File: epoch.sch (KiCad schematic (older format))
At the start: 30 parts, among them J1 USB_OTG, J2 CONN_01X05, P3 CONN_01X10, SW1 SW_Reset, SW2 SW_Up, SW3 SW_Middle, SW4 SW_Down, U1 MIC5219-3.3BM5, U2 ATSAMD21Ennc-AU, U3 DS3231MZ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

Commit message: Wire up
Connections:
- net INTC: now also U2.14 (PA11); no longer U2.25 (PA27)
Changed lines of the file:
@@
 Wire Wire Line
 	5550 2400 5550 2600
-Text GLabel 3750 5600 2    60   Input ~ 0
+Text GLabel 3750 4500 2    60   Input ~ 0
 INTC
 $EndSCHEMATC

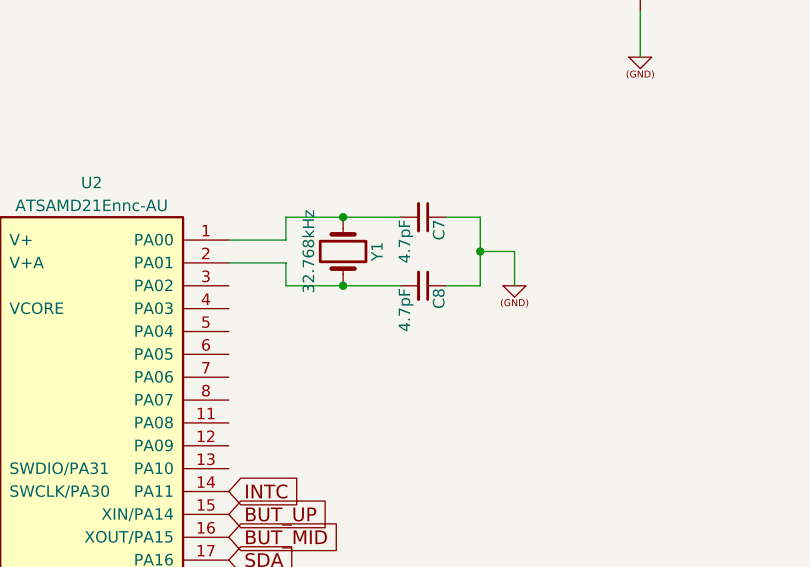
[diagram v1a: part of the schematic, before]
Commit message: Update resonator crystal to 18pF and create BOM csv
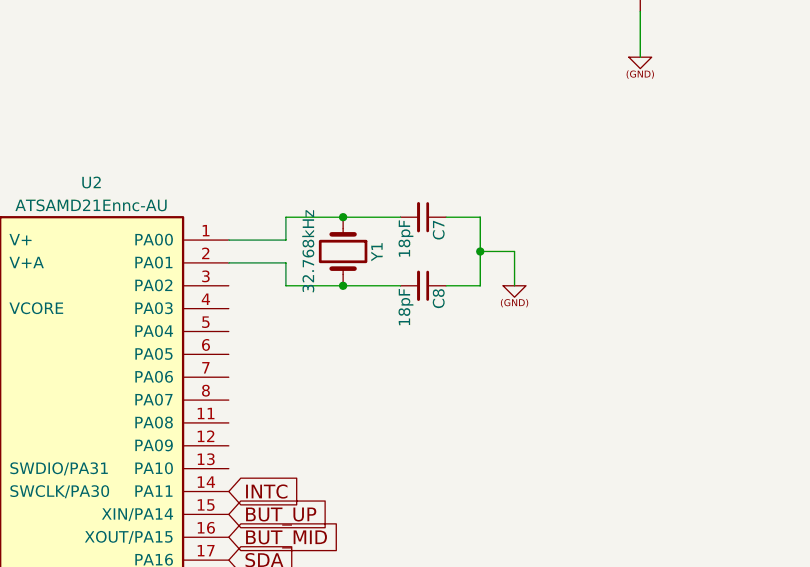
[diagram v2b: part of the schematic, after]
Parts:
- C7, C8: value 4.7pF -> 18pF
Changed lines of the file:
@@
 P 4600 3300
 F 0 "C7" H 4610 3370 50  0000 L CNN
-F 1 "4.7pF" H 4610 3220 50  0000 L CNN
+F 1 "18pF" H 4610 3220 50  0000 L CNN
 F 2 "Capacitors_SMD:C_0805_HandSoldering" H 4600 3300 50  0001 C CNN
 F 3 "" H 4600 3300 50  0000 C CNN
@@
 P 4600 3600
 F 0 "C8" H 4610 3670 50  0000 L CNN
-F 1 "4.7pF" H 4610 3520 50  0000 L CNN
+F 1 "18pF" H 4610 3520 50  0000 L CNN
 F 2 "Capacitors_SMD:C_0805_HandSoldering" H 4600 3600 50  0001 C CNN
 F 3 "" H 4600 3600 50  0000 C CNN

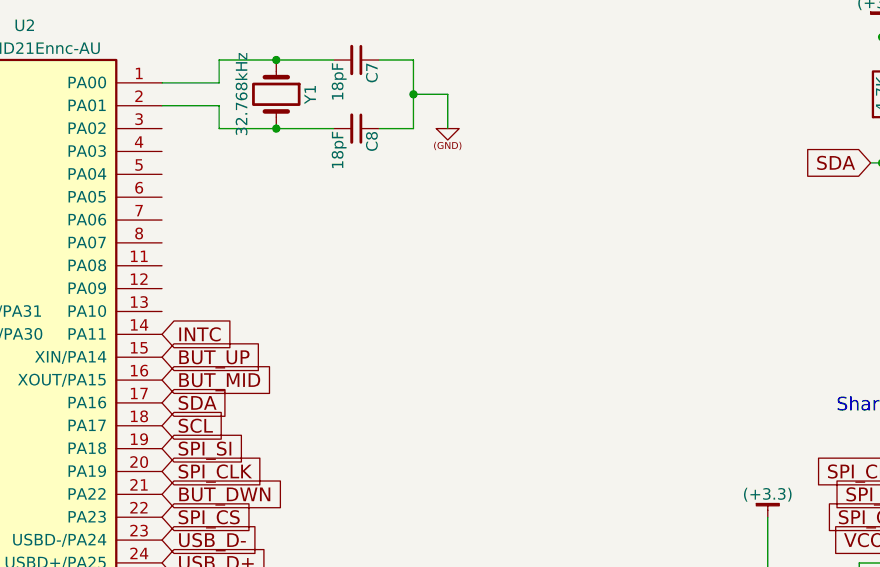
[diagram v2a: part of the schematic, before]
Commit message: Round corners and add LED
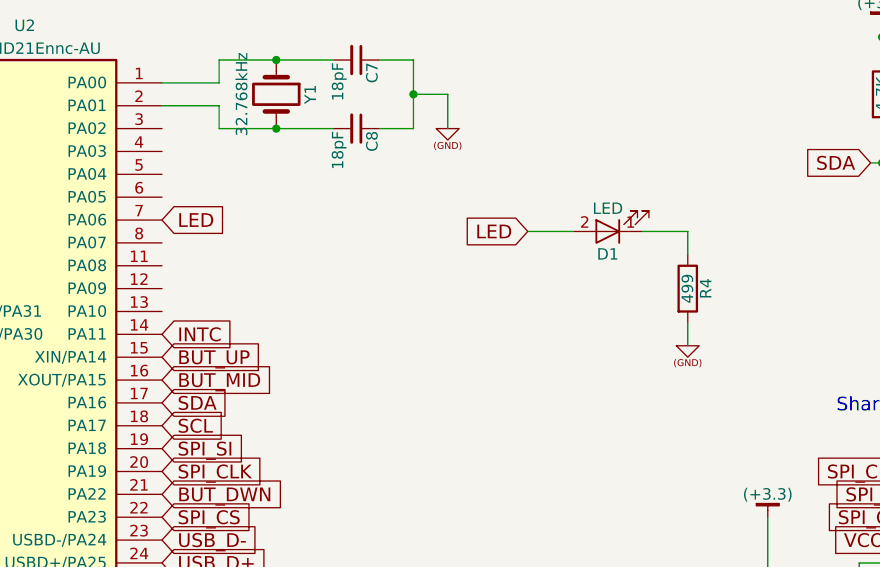
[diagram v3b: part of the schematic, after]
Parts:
- added D1: LED, LEDs:LED_0805, symbol LED
- added R4: 499, Resistors_SMD:R_0805_HandSoldering, symbol R
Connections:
- net (GND): now also R4.2
- net LED: now reaches U2.7 (PA06)
- net LED: now also D1.2 (A)
- new net: D1.1 (K), R4.1
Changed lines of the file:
@@
 Text GLabel 3750 4500 2    60   Input ~ 0
 INTC
+$Comp
+L LED D1
+U 1 1 590BD6CB
+P 5700 4050
+F 0 "D1" H 5700 4150 50  0000 C CNN
+F 1 "LED" H 5700 3950 50  0000 C CNN
+F 2 "LEDs:LED_0805" H 5700 4050 50  0001 C CNN
+F 3 "" H 5700 4050 50  0001 C CNN
+	1    5700 4050
+	-1   0    0    1
+$EndComp
+Text GLabel 3750 4000 2    60   Input ~ 0
+LED
+Text GLabel 5350 4050 0    60   Input ~ 0
+LED
+$Comp
+L R R4
+U 1 1 590BDF54
+P 6050 4300
+F 0 "R4" V 6130 4300 50  0000 C CNN
+F 1 "499" V 6050 4300 50  0000 C CNN
+F 2 "Resistors_SMD:R_0805_HandSoldering" V 5980 4300 50  0001 C CNN
+F 3 "" H 6050 4300 50  0000 C CNN
+	1    6050 4300
+	1    0    0    -1
+$EndComp
+$Comp
+L (GND) #PWR034
+U 1 1 590BE032
+P 6050 4550
+F 0 "#PWR034" H 6050 4550 30  0001 C CNN
+F 1 "(GND)" H 6050 4550 30  0001 C CNN
+F 2 "" H 6050 4550 60  0000 C CNN
+F 3 "" H 6050 4550 60  0000 C CNN
+	1    6050 4550
+	1    0    0    -1
+$EndComp
+Wire Wire Line
+	5350 4050 5550 4050
+Wire Wire Line
+	5850 4050 6050 4050
+Wire Wire Line
+	6050 4050 6050 4150
+Wire Wire Line
+	6050 4450 6050 4550
 $EndSCHEMATC
